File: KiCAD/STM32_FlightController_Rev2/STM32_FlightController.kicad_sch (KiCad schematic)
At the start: 56 parts, among them J1 629105150521, J2 JST_SH_SM08B-SRSS-TB_1x08-1MP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, J3 JST_SH_SM04B-SRSS-TB_1x04-1MP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, J4 JST_SH_SM04B-SRSS-TB_1x04-1MP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, J5 Conn_02x05_Odd_Even, SW1 PTS815SJM250SMTRLFS, SW2 PCM12SMTR, U1 SN74LVC1T45DBV, U2 ICM-20948, U3 STM32F405RGTx, U4 USBLC6-2SC6, U5 AMS1117-3.3, U6 TLV70018, U7 BMP390L, U8 SN74LVC1T45DBV, Y1 X32258MOB4SI

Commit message: replaced mounting holes with padded ones
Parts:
- removed H1, H2, H3, H4: MountingHole, MountingHole:MountingHole_4mm, symbol Mechanical:MountingHole
- added H1, H2, H3, H4: MountingHole_Pad, MountingHole:MountingHole_4mm_Pad, symbol Mechanical:MountingHole_Pad
- renumbered C5 to C10, C6 to C11, C7 to C12, C17 to C13, C8 to C14, C18 to C15, C9 to C16, C13 to C17, C14 to C18, C10 to C19, C21 to C2, C15 to C20, C11 to C21, C12 to C22, C16 to C23, C2 to C3, C19 to C4, C22 to C5, C3 to C6, C23 to C7, C4 to C8, C20 to C9, D2 to D1, D1 to D2, J4 to J3, J3 to J4, R10 to R1, R8 to R10, R9 to R2, R1 to R3, R3 to R4, R6 to R5, R2 to R6, R4 to R7, R7 to R8, R5 to R9, U4 to U1, U5 to U2, U6 to U3, U3 to U4, U1 to U5, U8 to U6, U2 to U8
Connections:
- no-connect marks 36 -> 40

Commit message: minor positioning changes
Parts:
- renumbered C19 to C10, C21 to C11, C22 to C12, C17 to C13, C18 to C14, C20 to C15, C23 to C16, C13 to C17, C15 to C18, C4 to C19, C3 to C2, C9 to C20, C2 to C21, C5 to C22, C7 to C23, C6 to C3, C8 to C4, C10 to C5, C11 to C6, C12 to C7, C14 to C8, C16 to C9, D2 to D1, D1 to D2, J4 to J3, J3 to J4, R3 to R1, R1 to R10, R6 to R2, R4 to R3, R7 to R4, R9 to R5, R5 to R6, R8 to R7, R10 to R8, R2 to R9, U5 to U1, U8 to U2, U4 to U3, U1 to U4, U2 to U5, U3 to U6, U6 to U8

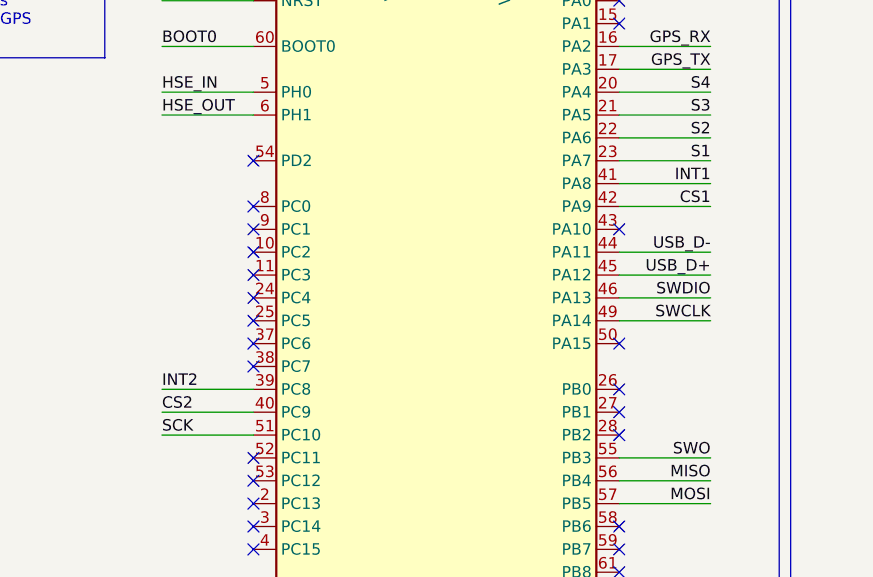
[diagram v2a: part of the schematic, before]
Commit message: cubeIDE code generation/setup
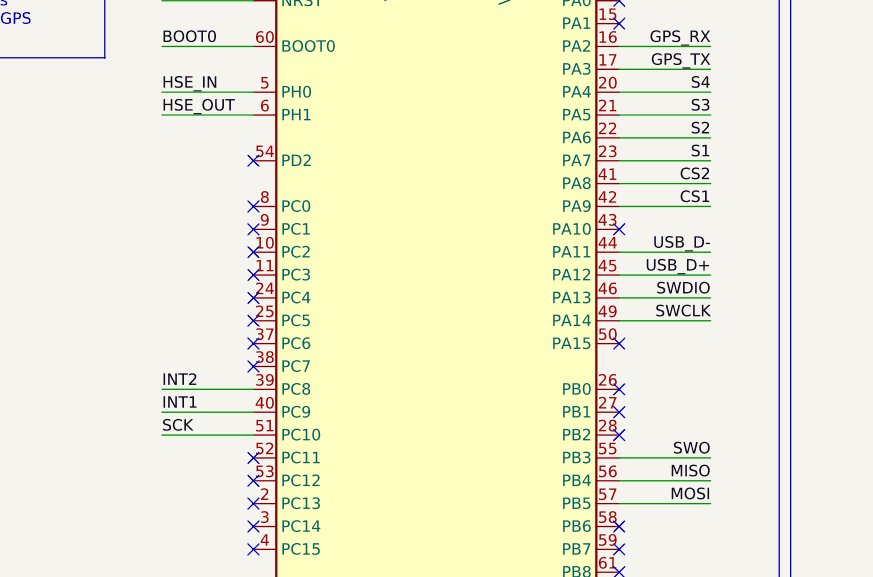
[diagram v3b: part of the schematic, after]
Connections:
- net CS2: now also U3.41 (PA8); no longer U3.40 (PC9)
- net INT1: now also U3.40 (PC9); no longer U3.41 (PA8)
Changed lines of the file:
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@@
 	(wire
 		(pts
-			(xy 185.42 78.74) (xy 195.58 78.74)
-		)
-		(stroke
-			(width 0)
-			(type default)
-		)
-	)
-	(wire
-		(pts
 			(xy 279.4 71.12) (xy 283.21 71.12)
 		)
@@
 	(wire
 		(pts
+			(xy 246.38 53.34) (xy 236.22 53.34)
+		)
+		(stroke
+			(width 0)
+			(type default)
+		)
+	)
+	(wire
+		(pts
 			(xy 101.6 156.21) (xy 106.68 156.21)
 		)
@@
 	(wire
 		(pts
-			(xy 246.38 53.34) (xy 236.22 53.34)
-		)
-		(stroke
-			(width 0)
-			(type default)
-		)
-	)
-	(wire
-		(pts
 			(xy 19.05 143.51) (xy 19.05 156.21)
 		)
@@
 	(wire
 		(pts
+			(xy 185.42 78.74) (xy 195.58 78.74)
+		)
+		(stroke
+			(width 0)
+			(type default)
+		)
+	)
+	(wire
+		(pts
 			(xy 39.37 156.21) (xy 49.53 156.21)
 		)
@@
 		)
 	)
-	(label "INT1"
-		(at 246.38 53.34 180)
-		(effects
-			(font
-				(size 1.27 1.27)
-			)
-			(justify right bottom)
-		)
-	)
 	(label "GPS_TX"
 		(at 246.38 40.64 180)
@@
 		)
 	)
+	(label "INT1"
+		(at 185.42 78.74 0)
+		(effects
+			(font
+				(size 1.27 1.27)
+			)
+			(justify left bottom)
+		)
+	)
 	(label "S1"
 		(at 246.38 50.8 180)
@@
 	)
 	(label "CS2"
+		(at 246.38 53.34 180)
+		(effects
+			(font
+				(size 1.27 1.27)
+			)
+			(justify right bottom)
+		)
+	)
+	(label "CS2"
 		(at 318.77 106.68 0)
 		(effects
@@
 		)
 	)
-	(label "CS2"
-		(at 185.42 78.74 0)
-		(effects
-			(font
-				(size 1.27 1.27)
-			)
-			(justify left bottom)
-		)
-	)

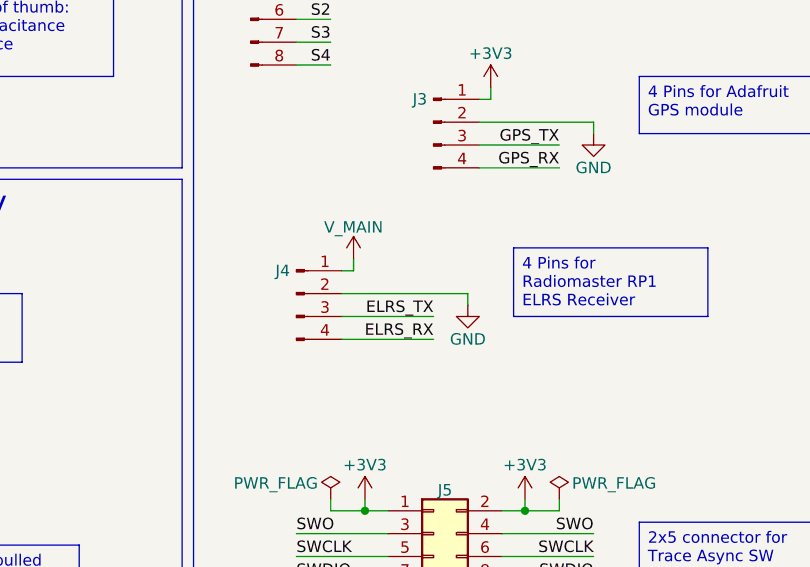
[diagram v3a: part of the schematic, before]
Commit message: swapped 5V and GND on the ELRS receiver connector
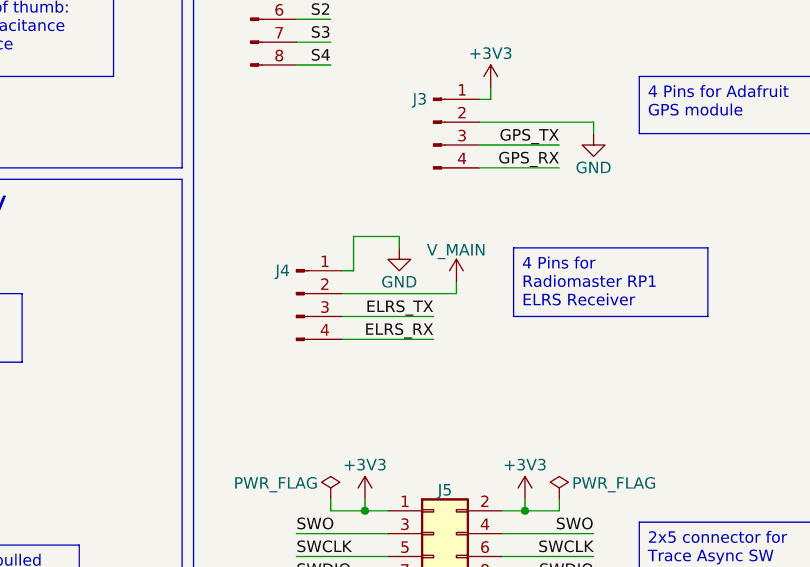
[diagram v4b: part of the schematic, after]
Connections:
- net GND: now also J4.1 (Pin_1); no longer J4.2 (Pin_2)
- net V_MAIN: now also J4.2 (Pin_2); no longer J4.1 (Pin_1)
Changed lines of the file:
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@@
 	(wire
 		(pts
-			(xy 107.95 189.23) (xy 106.68 189.23)
-		)
-		(stroke
-			(width 0)
-			(type default)
-		)
-	)
-	(wire
-		(pts
 			(xy 213.36 22.86) (xy 215.9 22.86)
 		)
@@
 	(wire
 		(pts
-			(xy 106.68 191.77) (xy 120.65 191.77)
-		)
-		(stroke
-			(width 0)
-			(type default)
-		)
-	)
-	(wire
-		(pts
 			(xy 185.42 76.2) (xy 195.58 76.2)
 		)
@@
 	(wire
 		(pts
+			(xy 119.38 191.77) (xy 106.68 191.77)
+		)
+		(stroke
+			(width 0)
+			(type default)
+		)
+	)
+	(wire
+		(pts
 			(xy 93.98 34.29) (xy 93.98 35.56)
 		)
@@
 	(wire
 		(pts
+			(xy 107.95 189.23) (xy 107.95 185.42)
+		)
+		(stroke
+			(width 0)
+			(type default)
+		)
+	)
+	(wire
+		(pts
 			(xy 220.98 22.86) (xy 220.98 25.4)
 		)
@@
 	(wire
 		(pts
-			(xy 120.65 191.77) (xy 120.65 193.04)
+			(xy 45.72 119.38) (xy 60.96 119.38)
 		)
 		(stroke
@@
 	(wire
 		(pts
-			(xy 45.72 119.38) (xy 60.96 119.38)
+			(xy 373.38 118.11) (xy 373.38 123.19)
 		)
 		(stroke
@@
 	(wire
 		(pts
-			(xy 373.38 118.11) (xy 373.38 123.19)
+			(xy 274.32 45.72) (xy 274.32 52.07)
 		)
 		(stroke
@@
 	(wire
 		(pts
-			(xy 274.32 45.72) (xy 274.32 52.07)
+			(xy 22.86 220.98) (xy 20.32 220.98)
 		)
 		(stroke
@@
 	(wire
 		(pts
-			(xy 22.86 220.98) (xy 20.32 220.98)
+			(xy 369.57 118.11) (xy 373.38 118.11)
 		)
 		(stroke
@@
 	(wire
 		(pts
-			(xy 369.57 118.11) (xy 373.38 118.11)
+			(xy 111.76 226.06) (xy 110.49 226.06)
 		)
 		(stroke
@@
 	(wire
 		(pts
-			(xy 111.76 226.06) (xy 110.49 226.06)
+			(xy 119.38 190.5) (xy 119.38 191.77)
+		)
+		(stroke
+			(width 0)
+			(type default)
+		)
+	)
+	(wire
+		(pts
+			(xy 113.03 185.42) (xy 113.03 186.69)
 		)
 		(stroke
@@
 	(wire
 		(pts
-			(xy 107.95 187.96) (xy 107.95 189.23)
+			(xy 288.29 29.21) (xy 289.56 29.21)
 		)
 		(stroke
@@
 	(wire
 		(pts
-			(xy 288.29 29.21) (xy 289.56 29.21)
+			(xy 33.02 71.12) (xy 34.29 71.12)
 		)
 		(stroke
@@
 	(wire
 		(pts
-			(xy 33.02 71.12) (xy 34.29 71.12)
+			(xy 111.76 215.9) (xy 109.22 215.9)
 		)
 		(stroke
@@
 	(wire
 		(pts
-			(xy 111.76 215.9) (xy 109.22 215.9)
+			(xy 290.83 86.36) (xy 298.45 86.36)
 		)
 		(stroke
@@
 	(wire
 		(pts
-			(xy 290.83 86.36) (xy 298.45 86.36)
+			(xy 121.92 172.72) (xy 134.62 172.72)
 		)
 		(stroke
@@
 	(wire
 		(pts
-			(xy 121.92 172.72) (xy 134.62 172.72)
+			(xy 33.02 223.52) (xy 40.64 223.52)
 		)
 		(stroke
@@
 	(wire
 		(pts
-			(xy 33.02 223.52) (xy 40.64 223.52)
+			(xy 106.68 189.23) (xy 107.95 189.23)
 		)
 		(stroke
@@
 	(wire
 		(pts
+			(xy 107.95 185.42) (xy 113.03 185.42)
+		)
+		(stroke
+			(width 0)
+			(type default)
+		)
+	)
+	(wire
+		(pts
 			(xy 275.59 45.72) (xy 274.32 45.72)
 		)
@@
 	(symbol
 		(lib_id "power:GND")
-		(at 120.65 193.04 0)
+		(at 113.03 186.69 0)
 		(unit 1)
 		(exclude_from_sim no)
@@
 		(dnp no)
 		(property "Reference" "#PWR048"
-			(at 120.65 199.39 0)
+			(at 113.03 193.04 0)
 			(effects
 				(font
@@
 		)
 		(property "Value" "GND"
-			(at 120.65 196.85 0)
+			(at 113.03 190.5 0)
 			(effects
 				(font
@@
 		)
 		(property "Footprint" ""
-			(at 120.65 193.04 0)
+			(at 113.03 186.69 0)
 			(effects
 				(font
@@
 		)
 		(property "Datasheet" ""
-			(at 120.65 193.04 0)
+			(at 113.03 186.69 0)
 			(effects
 				(font
@@
 		)
 		(property "Description" "Power symbol creates a global label with name \"GND\" , ground"
-			(at 120.65 193.04 0)
+			(at 113.03 186.69 0)
 			(effects
 				(font
@@
 	(symbol
 		(lib_id "power:+5V")
-		(at 107.95 187.96 0)
+		(at 119.38 190.5 0)
 		(unit 1)
 		(exclude_from_sim no)
@@
 		(dnp no)
 		(property "Reference" "#PWR047"
-			(at 107.95 191.77 0)
+			(at 119.38 194.31 0)
 			(effects
 				(font
@@
 		)
 		(property "Value" "V_MAIN"
-			(at 107.95 184.404 0)
+			(at 119.38 186.944 0)
 			(effects
 				(font
@@
 		)
 		(property "Footprint" ""
-			(at 107.95 187.96 0)
+			(at 119.38 190.5 0)
 			(effects
 				(font
@@
 		)
 		(property "Datasheet" ""
-			(at 107.95 187.96 0)
+			(at 119.38 190.5 0)
 			(effects
 				(font
@@
 		)
 		(property "Description" "Power symbol creates a global label with name \"+5V\""
-			(at 107.95 187.96 0)
+			(at 119.38 190.5 0)
 			(effects
 				(font
